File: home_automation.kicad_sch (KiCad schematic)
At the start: 44 parts, among them J1 AC In, J2 NodeMCU Header, J3 NodeMCU Header, J4 SW_4, J5 DHT11, J6 SW_1, J7 SW_3, J8 SW_2, K1 Relay_SPDT, K2 Relay_SPDT, K3 Relay_SPDT, K4 Relay_SPDT, Q1 D882, Q2 D882, Q3 D882, Q4 D882, U1 PC817, U2 PC817, U3 LM7805_TO220, U4 PC817, U5 PC817, U6 NodeMCU

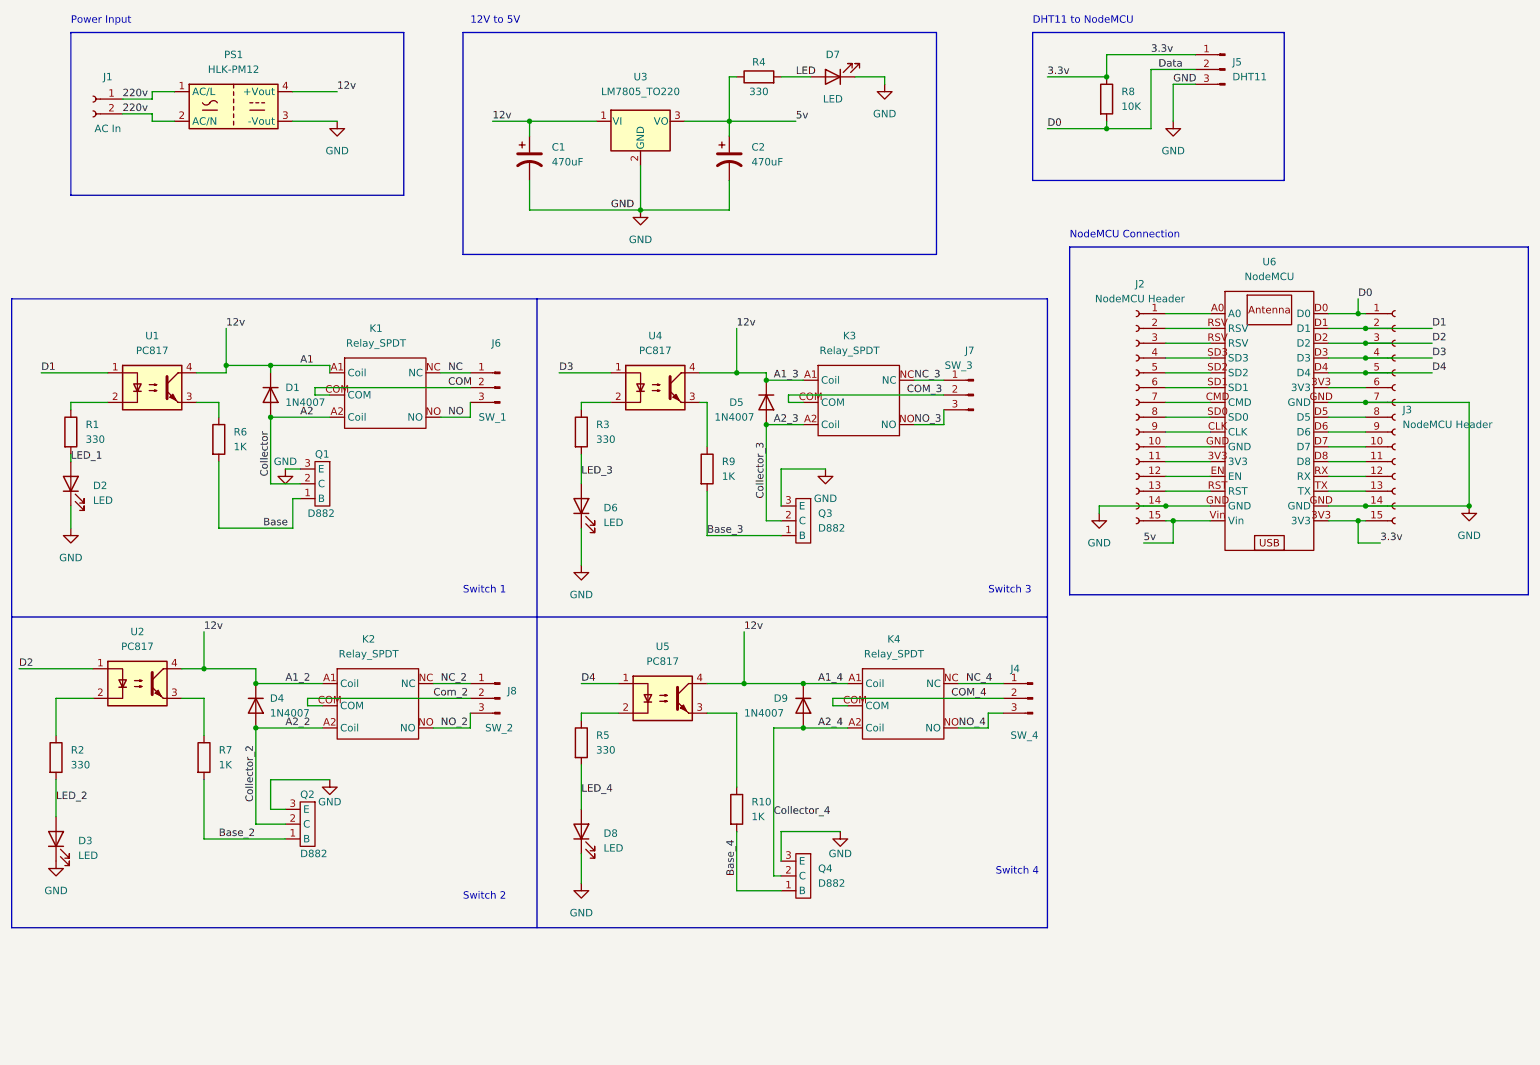
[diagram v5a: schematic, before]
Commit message: Correction done in schematic diagram
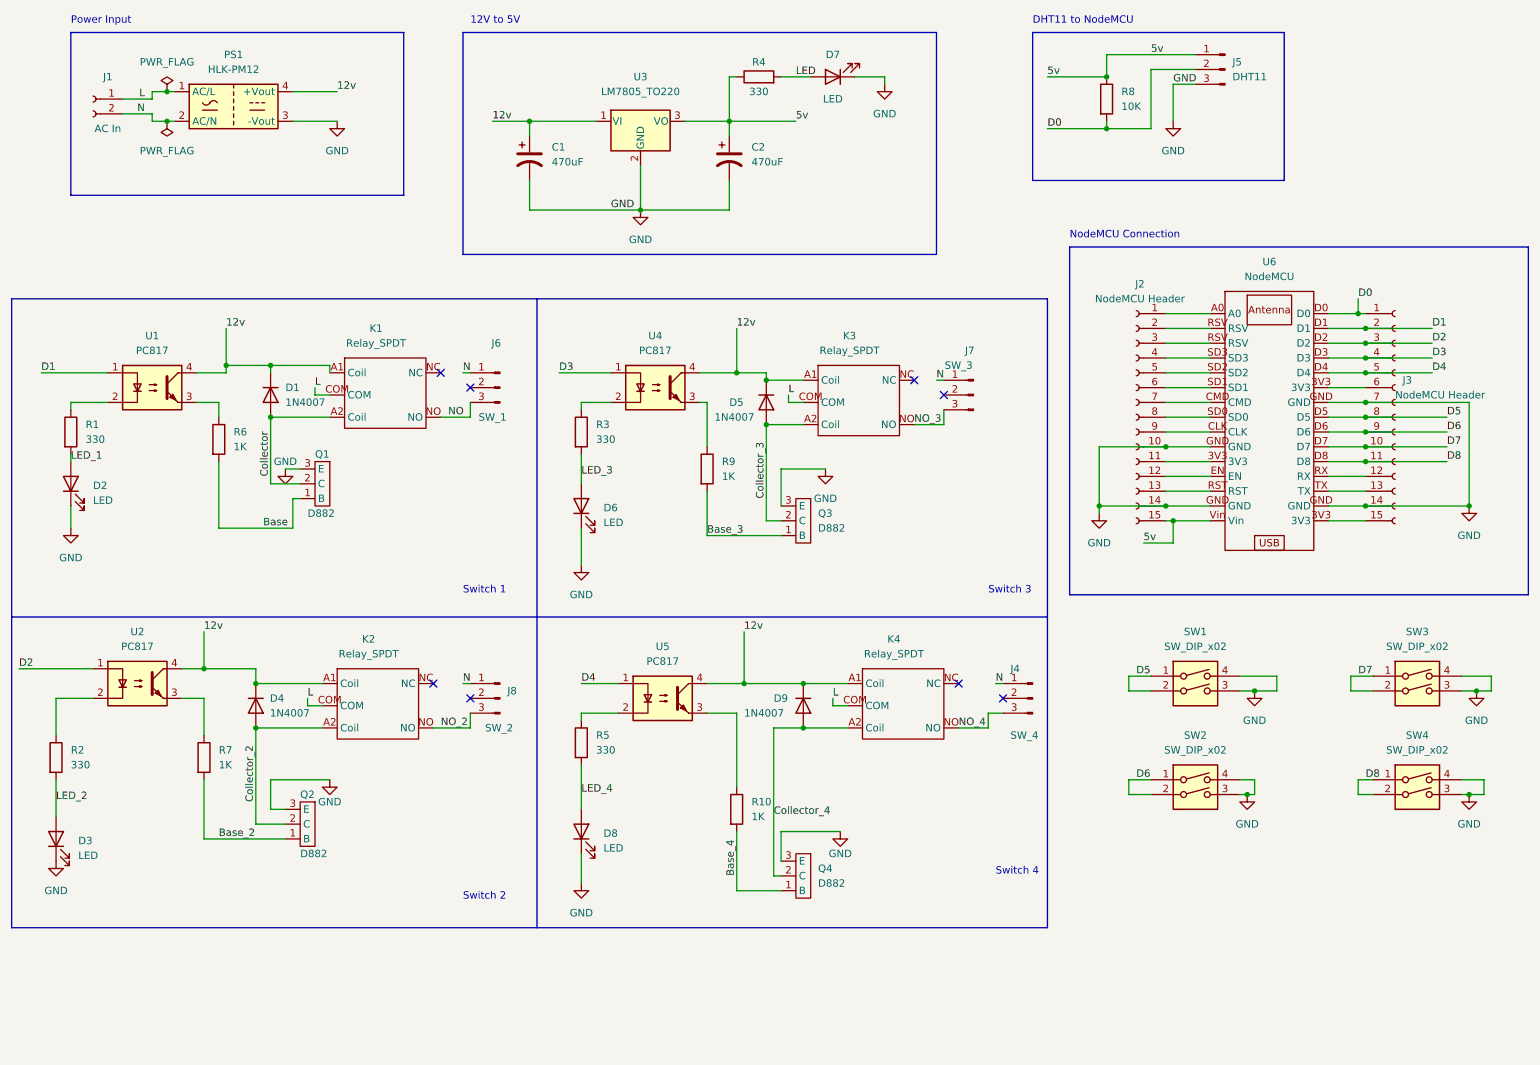
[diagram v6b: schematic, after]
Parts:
- added SW1, SW2, SW3, SW4: SW_DIP_x02, My_Footprints:4_pin_Button, symbol Switch:SW_DIP_x02
- C1, C2: footprint (none) -> Capacitor_THT:CP_Radial_D10.0mm_P5.00mm
- D2, D3, D6, D7, D8: footprint (none) -> LED_THT:LED_D3.0mm
- J1: footprint (none) -> Connector_PinHeader_2.54mm:PinHeader_1x02_P2.54mm_Vertical
- J2, J3: footprint (none) -> Connector_PinHeader_2.54mm:PinHeader_1x15_P2.54mm_Vertical
- J4, J6, J7, J8: footprint (none) -> Connector_Phoenix_MSTB:PhoenixContact_MSTBA_2,5_3-G_1x03_P5.00mm_Horizontal
- J5: footprint (none) -> Connector_PinHeader_2.54mm:PinHeader_1x03_P2.54mm_Vertical
- R1, R2, R3, R4, R5: footprint (none) -> Resistor_THT:R_Axial_DIN0414_L11.9mm_D4.5mm_P15.24mm_Horizontal
- R10, R6, R7, R8, R9: footprint (none) -> Resistor_THT:R_Axial_DIN0516_L15.5mm_D5.0mm_P25.40mm_Horizontal
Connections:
- net 5v: now also J5.1 (Pin_1), R8.1
- net GND: now also J2.10 (Pin_10), SW1.3, SW1.4, SW2.3, SW2.4, SW3.3, SW3.4, SW4.3, SW4.4
- net D7: now reaches J3.10 (Pin_10), U6.D7
- net D7: now also SW3.1, SW3.2
- net D8: now reaches J3.11 (Pin_11), U6.D8
- net D8: now also SW4.1, SW4.2
- net D5: now reaches J3.8 (Pin_8), U6.D5
- net D5: now also SW1.1, SW1.2
- net D6: now reaches J3.9 (Pin_9), U6.D6
- net D6: now also SW2.1, SW2.2
- net 220v renamed L
- net L: now also K1.COM, K2.COM, K3.COM, K4.COM; no longer J1.2 (Pin_2), PS1.2 (AC/N)
- removed net 3.3v: J3.15 (Pin_15), J5.1 (Pin_1), R8.1, U6.3V3
- net A2 renamed Collector
- net A2_2 renamed Collector_2
- net A2_3 renamed Collector_3
- net A2_4 renamed Collector_4
- net COM: no longer names the net of J6.2 (Pin_2)
- net COM: no longer K1.COM
- net COM_3: no longer names the net of J7.2 (Pin_2)
- net COM_3: no longer K3.COM
- net COM_4: no longer names the net of J4.2 (Pin_2)
- net COM_4: no longer K4.COM
- net Com_2: no longer names the net of J8.2 (Pin_2)
- net Com_2: no longer K2.COM
- net NC: no longer names the net of K1.NC
- net NC: no longer J6.1 (Pin_1)
- net NC_2: no longer names the net of K2.NC
- net NC_2: no longer J8.1 (Pin_1)
- net NC_3: no longer names the net of K3.NC
- net NC_3: no longer J7.1 (Pin_1)
- net NC_4: no longer names the net of K4.NC
- net NC_4: no longer J4.1 (Pin_1)
- new net: J3.15 (Pin_15), U6.3V3
- new net N: J1.2 (Pin_2), J4.1 (Pin_1), J6.1 (Pin_1), J7.1 (Pin_1), J8.1 (Pin_1), PS1.2 (AC/N)
- no-connect marks 0 -> 8

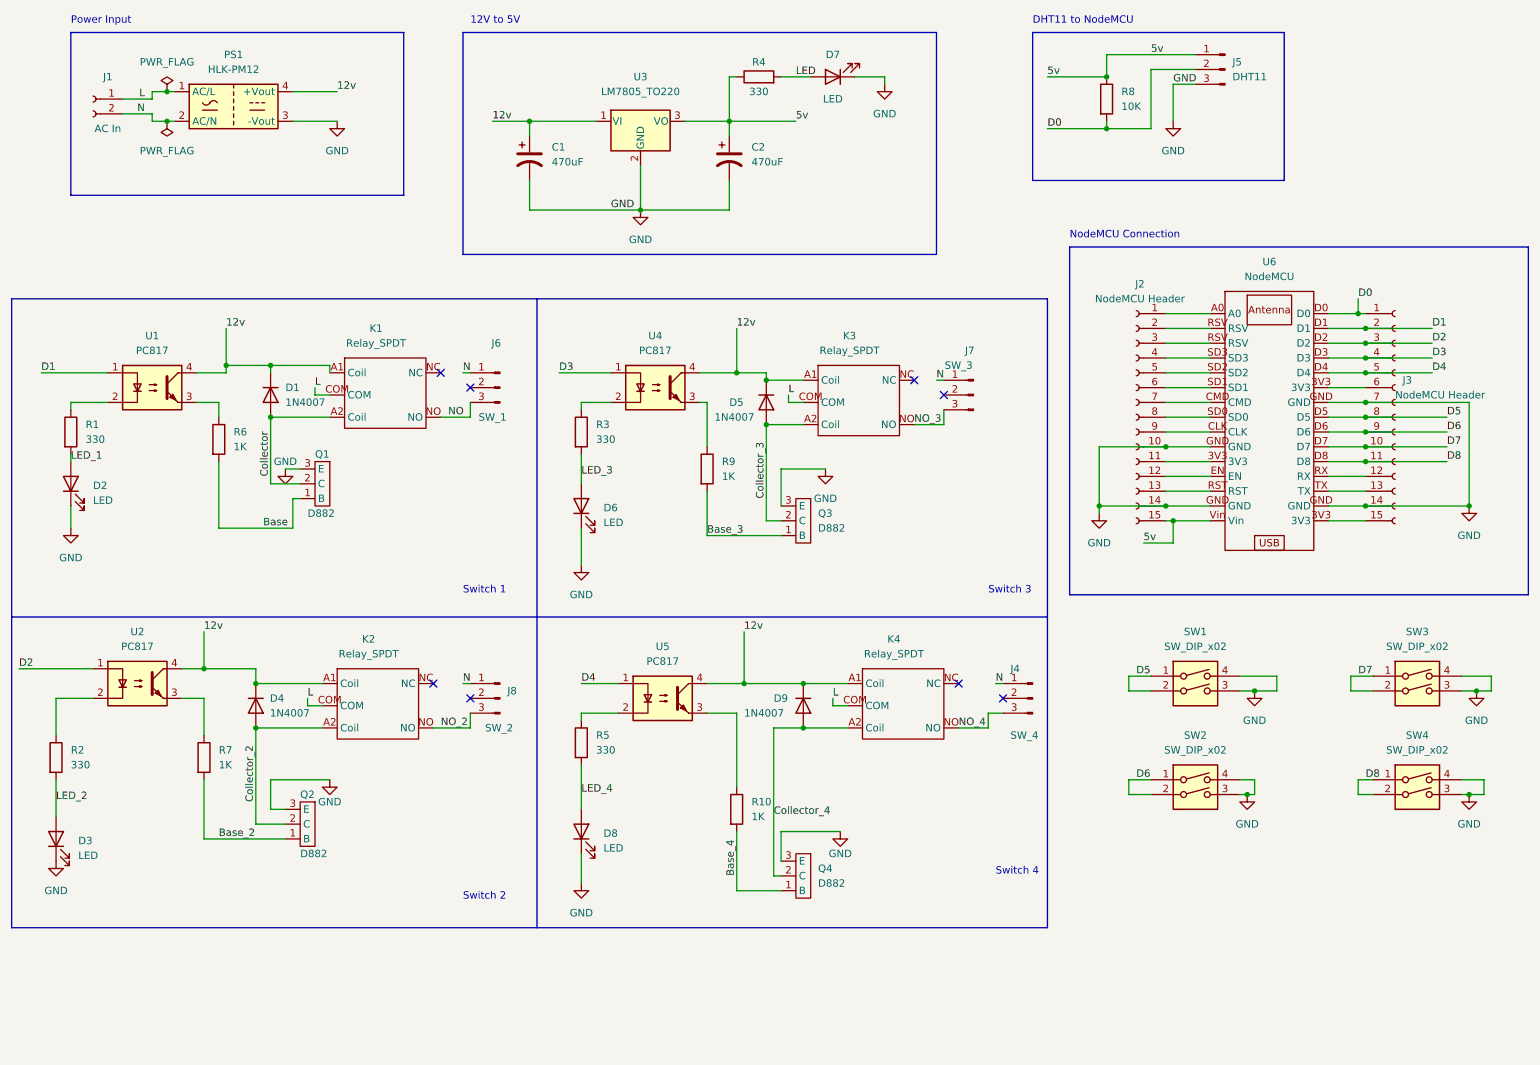
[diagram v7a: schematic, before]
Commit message: Replaced connectors
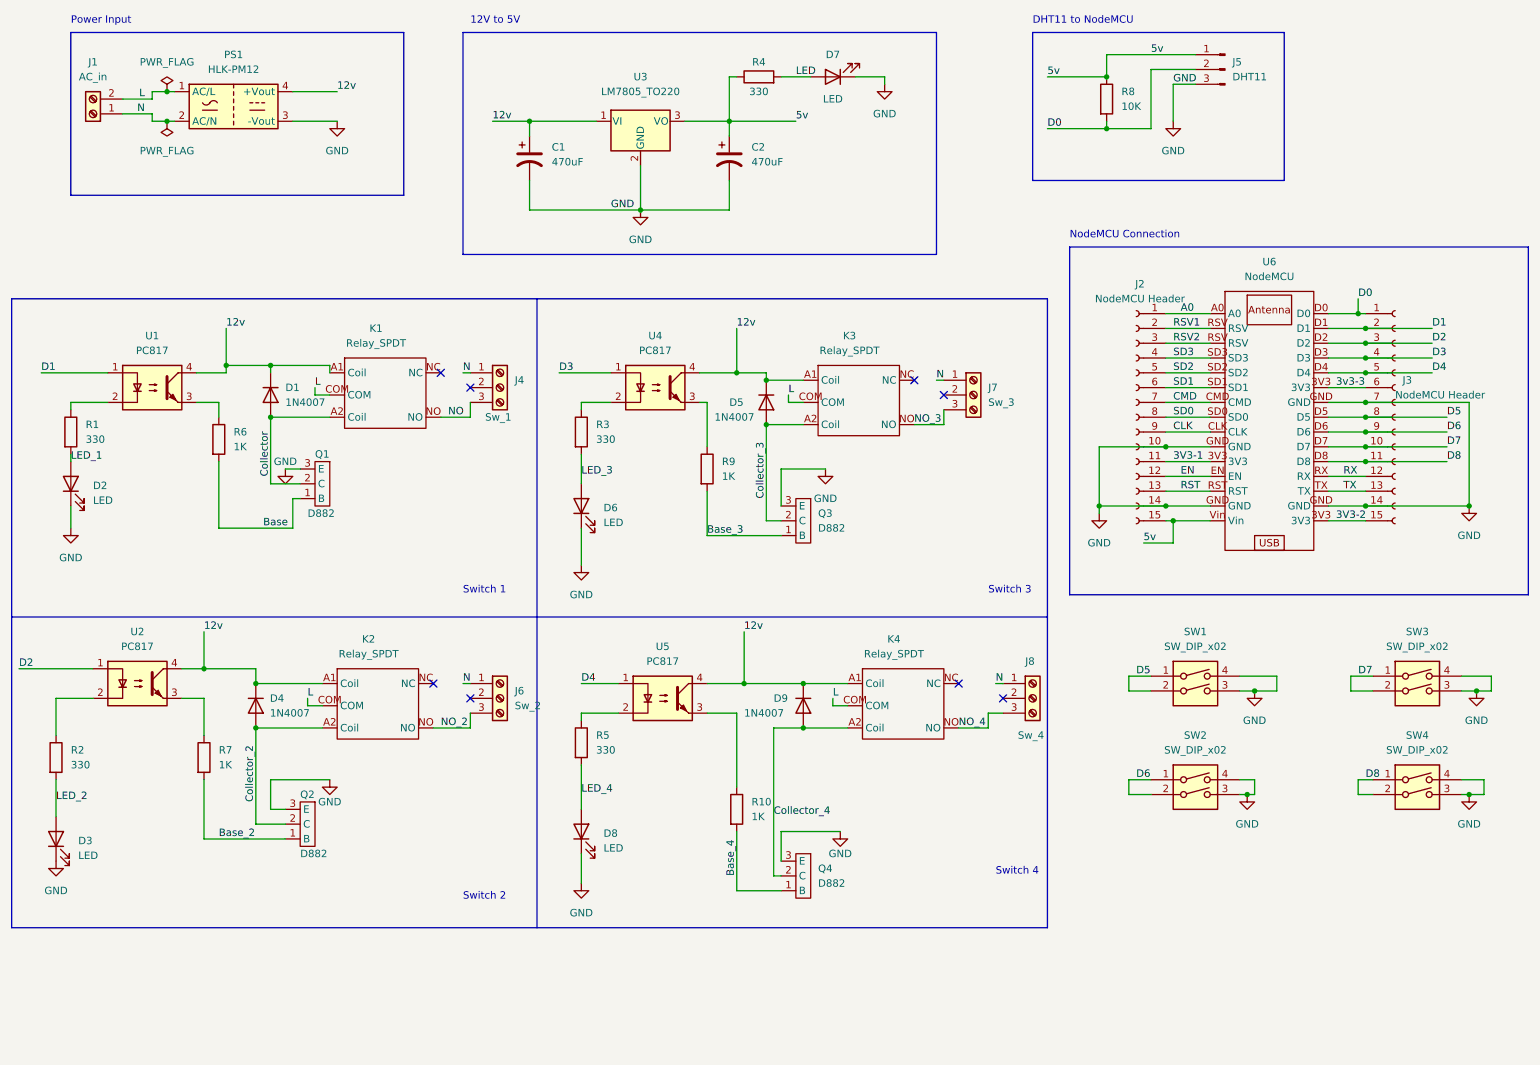
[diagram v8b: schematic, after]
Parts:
- removed J1: AC In, Connector_PinHeader_2.54mm:PinHeader_1x02_P2.54mm_Vertical, symbol Connector:Conn_01x02_Female
- removed J4: SW_4, Connector_Phoenix_MSTB:PhoenixContact_MSTBA_2,5_3-G_1x03_P5.00mm_Horizontal, symbol Connector:Conn_01x03_Male
- removed J6: SW_1, Connector_Phoenix_MSTB:PhoenixContact_MSTBA_2,5_3-G_1x03_P5.00mm_Horizontal, symbol Connector:Conn_01x03_Male
- removed J7: SW_3, Connector_Phoenix_MSTB:PhoenixContact_MSTBA_2,5_3-G_1x03_P5.00mm_Horizontal, symbol Connector:Conn_01x03_Male
- removed J8: SW_2, Connector_Phoenix_MSTB:PhoenixContact_MSTBA_2,5_3-G_1x03_P5.00mm_Horizontal, symbol Connector:Conn_01x03_Male
- added J1: AC_in, TerminalBlock:TerminalBlock_bornier-2_P5.08mm, symbol Connector:Screw_Terminal_01x02
- added J4: Sw_1, TerminalBlock:TerminalBlock_bornier-3_P5.08mm, symbol Connector:Screw_Terminal_01x03
- added J6: Sw_2, TerminalBlock:TerminalBlock_bornier-3_P5.08mm, symbol Connector:Screw_Terminal_01x03
- added J7: Sw_3, TerminalBlock:TerminalBlock_bornier-3_P5.08mm, symbol Connector:Screw_Terminal_01x03
- added J8: Sw_4, TerminalBlock:TerminalBlock_bornier-3_P5.08mm, symbol Connector:Screw_Terminal_01x03
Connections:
- net L: now also J1.2 (Pin_2)
- net N: now also J1.1 (Pin_1), J4.1 (Pin_1), J6.1 (Pin_1), J7.1 (Pin_1), J8.1 (Pin_1)
- net NO: now also J4.3 (Pin_3)
- net NO_2: now also J6.3 (Pin_3)
- net NO_3: now also J7.3 (Pin_3)
- net NO_4: now also J8.3 (Pin_3)
- net A0: now reaches J2.1 (Pin_1), U6.A0
- net 3V3-1: now reaches J2.11 (Pin_11), U6.3V3
- net EN: now reaches J2.12 (Pin_12), U6.EN
- net RST: now reaches J2.13 (Pin_13), U6.RST
- net RSV1: now reaches J2.2 (Pin_2), U6.RSV
- net RSV2: now reaches J2.3 (Pin_3), U6.RSV
- net SD3: now reaches J2.4 (Pin_4), U6.SD3
- net SD2: now reaches J2.5 (Pin_5), U6.SD2
- net SD1: now reaches J2.6 (Pin_6), U6.SD1
- net CMD: now reaches J2.7 (Pin_7), U6.CMD
- net SD0: now reaches J2.8 (Pin_8), U6.SD0
- net CLK: now reaches J2.9 (Pin_9), U6.CLK
- net RX: now reaches J3.12 (Pin_12), U6.RX
- net TX: now reaches J3.13 (Pin_13), U6.TX
- net 3V3-2: now reaches J3.15 (Pin_15), U6.3V3
- net 3v3-3: now reaches J3.6 (Pin_6), U6.3V3
